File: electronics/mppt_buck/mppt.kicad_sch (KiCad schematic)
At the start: 50 parts, among them J1 I2C, J2 UART, J3 In, J4 In, J5 Out, J6 Out, Q1 IRLR2705TRPBF, Q2 IRLR2705TRPBF, SW1 SW_DIP_x01, U1 AD8211, U2 AD8211, U3 ATmega328P-A, U4 2EDN852x, U5 L78L15_SO8, Y1 16.00M-SMDHC49S

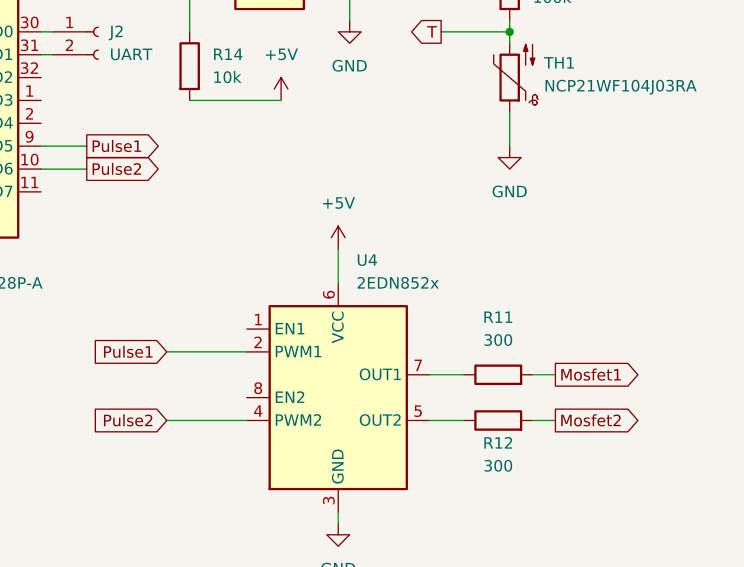
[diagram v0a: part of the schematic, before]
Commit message: links fixed
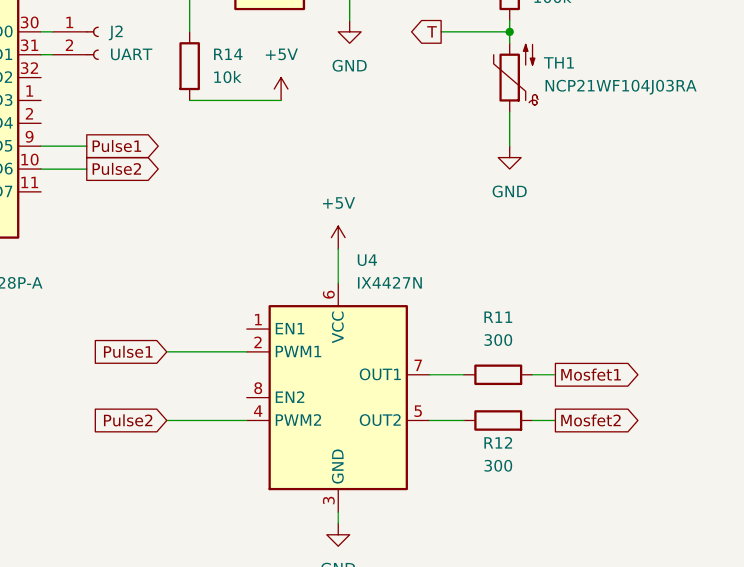
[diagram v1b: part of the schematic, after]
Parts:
- U4: value 2EDN852x -> IX4427N
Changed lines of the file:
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@@
       (effects (font (size 1.27 1.27)) hide)
     )
-    (property "Datasheet" "https://www.tme.eu/pl/details/t491d106k050at/kondensatory-tantalowe-smd/kemet/" (id 3) (at 33.02 137.16 0)
+    (property "Datasheet" "https://www.tme.eu/pl/details/vs1h100mc054000ce0/kondensatory-elektrolityczne-smd/changzhou-huawei-electronic/" (id 3) (at 33.02 137.16 0)
       (effects (font (size 1.27 1.27)) hide)
     )
@@
       (effects (font (size 1.27 1.27)) hide)
     )
-    (property "Datasheet" "https://www.tme.eu/pl/details/t491x226k050at/kondensatory-tantalowe-smd/kemet/" (id 3) (at 104.14 139.7 0)
+    (property "Datasheet" "https://www.tme.eu/pl/details/eee1ha220wp/kondensatory-elektrolityczne-smd/panasonic/" (id 3) (at 104.14 139.7 0)
       (effects (font (size 1.27 1.27)) hide)
     )
@@
       (effects (font (size 1.27 1.27)) hide)
     )
-    (property "Datasheet" "https://www.tme.eu/pl/details/t491d106k050at/kondensatory-tantalowe-smd/kemet/" (id 3) (at 31.75 66.04 0)
+    (property "Datasheet" "https://www.tme.eu/pl/details/vs1h100mc054000ce0/kondensatory-elektrolityczne-smd/changzhou-huawei-electronic/" (id 3) (at 31.75 66.04 0)
       (effects (font (size 1.27 1.27)) hide)
     )
@@
       (effects (font (size 1.27 1.27)) hide)
     )
-    (property "Datasheet" "https://www.tme.eu/pl/details/t491x226k050at/kondensatory-tantalowe-smd/kemet/" (id 3) (at 102.87 68.58 0)
+    (property "Datasheet" "https://www.tme.eu/pl/details/eee1ha220wp/kondensatory-elektrolityczne-smd/panasonic/" (id 3) (at 102.87 68.58 0)
       (effects (font (size 1.27 1.27)) hide)
     )
@@
       (effects (font (size 1.27 1.27) italic) hide)
     )
-    (property "Datasheet" "http://www.st.com/content/ccc/resource/technical/document/datasheet/15/55/e5/aa/23/5b/43/fd/CD00000446.pdf/files/CD00000446.pdf/jcr:content/translations/en.CD00000446.pdf" (id 3) (at 267.97 46.99 0)
+    (property "Datasheet" "https://www.tme.eu/pl/details/l78l15cd-tr/stabilizatory-napiecia-nieregulowane/stmicroelectronics/" (id 3) (at 267.97 46.99 0)
       (effects (font (size 1.27 1.27)) hide)
     )
@@
       (effects (font (size 1.27 1.27)) (justify left))
     )
-    (property "Value" "2EDN852x" (id 1) (at 247.1294 113.03 0)
+    (property "Value" "IX4427N" (id 1) (at 247.1294 113.03 0)
       (effects (font (size 1.27 1.27)) (justify left))
     )
@@
       (effects (font (size 1.27 1.27)) hide)
     )
-    (property "Datasheet" "http://www.st.com/resource/en/datasheet/pm8834.pdf" (id 3) (at 245.11 125.73 0)
+    (property "Datasheet" "https://www.tme.eu/pl/details/ix4427n/drivery-mosfet-igbt/ixys/" (id 3) (at 245.11 125.73 0)
       (effects (font (size 1.27 1.27)) hide)
     )
@@
     )
     (path "/f34564fb-d64a-449a-883e-a3d54ee9a0c7"
-      (reference "U4") (unit 1) (value "2EDN852x") (footprint "Package_SO:SOIC-8_3.9x4.9mm_P1.27mm")
+      (reference "U4") (unit 1) (value "IX4427N") (footprint "Package_SO:SOIC-8_3.9x4.9mm_P1.27mm")
     )
     (path "/e1c2f98d-65b5-4f1f-ae31-d3d1a6b636f5"

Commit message: links almost fixed finally
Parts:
- U1, U2: value AD8211 -> INA180A4IDBVT
- U5: value L78L15_SO8 -> DI78L05DAB
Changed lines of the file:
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@@
     (in_bom yes) (on_board yes) (fields_autoplaced)
     (property "Reference" "U2" (id 0) (at 105.41 98.3105 0))
-    (property "Value" "AD8211" (id 1) (at 105.41 100.8505 0))
+    (property "Value" "INA180A4IDBVT" (id 1) (at 105.41 100.8505 0))
     (property "Footprint" "Package_TO_SOT_SMD:SOT-23-5" (id 2) (at 118.11 109.22 0)
       (effects (font (size 1.27 1.27)) hide)
     )
-    (property "Datasheet" "https://www.tme.eu/pl/details/ad8211yrjz-r2/wzmacniacze-operacyjne-smd/analog-devices/" (id 3) (at 134.62 91.44 0)
+    (property "Datasheet" "https://www.tme.eu/pl/details/ina180a4idbvt/wzmacniacze-operacyjne-smd/texas-instruments/" (id 3) (at 134.62 91.44 0)
       (effects (font (size 1.27 1.27)) hide)
     )
@@
     (in_bom yes) (on_board yes) (fields_autoplaced)
     (property "Reference" "U1" (id 0) (at 104.14 27.1905 0))
-    (property "Value" "AD8211" (id 1) (at 104.14 29.7305 0))
+    (property "Value" "INA180A4IDBVT" (id 1) (at 104.14 29.7305 0))
     (property "Footprint" "Package_TO_SOT_SMD:SOT-23-5" (id 2) (at 116.84 38.1 0)
       (effects (font (size 1.27 1.27)) hide)
     )
-    (property "Datasheet" "https://www.tme.eu/pl/details/ad8211yrjz-r2/wzmacniacze-operacyjne-smd/analog-devices/" (id 3) (at 133.35 20.32 0)
+    (property "Datasheet" "https://www.tme.eu/pl/details/ina180a4idbvt/wzmacniacze-operacyjne-smd/texas-instruments/" (id 3) (at 133.35 20.32 0)
       (effects (font (size 1.27 1.27)) hide)
     )
@@
     (in_bom yes) (on_board yes) (fields_autoplaced)
     (property "Reference" "U5" (id 0) (at 262.89 39.37 0))
-    (property "Value" "L78L15_SO8" (id 1) (at 262.89 41.91 0))
+    (property "Value" "DI78L05DAB" (id 1) (at 262.89 41.91 0))
     (property "Footprint" "Package_SO:SOIC-8_3.9x4.9mm_P1.27mm" (id 2) (at 265.43 41.91 0)
       (effects (font (size 1.27 1.27) italic) hide)
     )
-    (property "Datasheet" "https://www.tme.eu/pl/details/l78l15cd-tr/stabilizatory-napiecia-nieregulowane/stmicroelectronics/" (id 3) (at 267.97 46.99 0)
+    (property "Datasheet" "https://www.tme.eu/pl/details/di78l05dab-dio/stabilizatory-napiecia-nieregulowane/diotec-semiconductor/di78l05dab/" (id 3) (at 267.97 46.99 0)
       (effects (font (size 1.27 1.27)) hide)
     )
@@
     )
     (path "/98f6b66c-5996-461c-b7fb-355b97b82833"
-      (reference "U1") (unit 1) (value "AD8211") (footprint "Package_TO_SOT_SMD:SOT-23-5")
+      (reference "U1") (unit 1) (value "INA180A4IDBVT") (footprint "Package_TO_SOT_SMD:SOT-23-5")
     )
     (path "/4613b16e-f85f-4ff8-be22-af836321faaf"
-      (reference "U2") (unit 1) (value "AD8211") (footprint "Package_TO_SOT_SMD:SOT-23-5")
+      (reference "U2") (unit 1) (value "INA180A4IDBVT") (footprint "Package_TO_SOT_SMD:SOT-23-5")
     )
     (path "/4efefe47-8389-4ee5-9e21-0623814e6216"
@@
     )
     (path "/e1c2f98d-65b5-4f1f-ae31-d3d1a6b636f5"
-      (reference "U5") (unit 1) (value "L78L15_SO8") (footprint "Package_SO:SOIC-8_3.9x4.9mm_P1.27mm")
+      (reference "U5") (unit 1) (value "DI78L05DAB") (footprint "Package_SO:SOIC-8_3.9x4.9mm_P1.27mm")
     )
     (path "/4fe02d41-b24c-4ab7-a3f5-8f451d9bcad9"

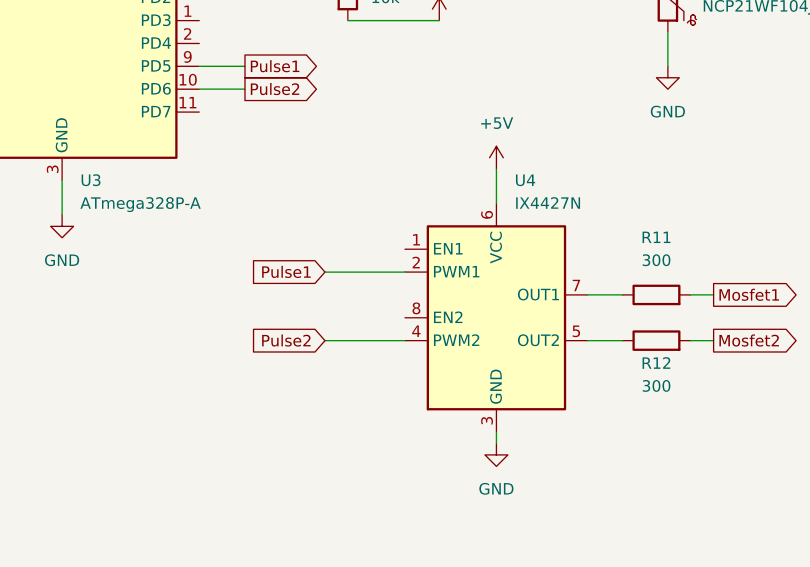
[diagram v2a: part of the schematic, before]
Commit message: mppt part list corrected
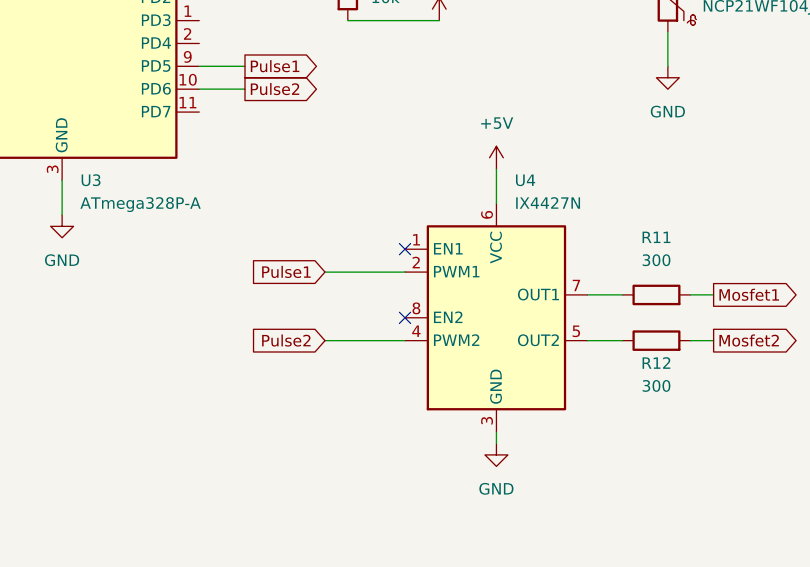
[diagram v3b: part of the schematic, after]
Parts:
- C1, C2: footprint Capacitor_Tantalum_SMD:CP_EIA-7343-15_Kemet-W_Pad2.25x2.55mm_HandSolder -> Capacitor_SMD:CP_Elec_5x5.4
- C3, C4: footprint Capacitor_Tantalum_SMD:CP_EIA-7343-15_Kemet-W_Pad2.25x2.55mm_HandSolder -> Capacitor_SMD:CP_Elec_6.3x5.4
- L1, L2: footprint Inductor_SMD:L_Bourns_SRR1208_12.7x12.7mm -> Inductor_SMD:L_10.4x10.4_H4.8
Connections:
- no-connect marks 0 -> 2
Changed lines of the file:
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@@
   (junction (at 82.55 67.31) (diameter 0) (color 0 0 0 0)
   )
+  (no_connect (at 234.95 118.11))
+  (no_connect (at 234.95 125.73))
   (wire (pts (xy 212.09 67.31) (xy 217.17 67.31))
     (stroke (width 0) (type default) (color 0 0 0 0))
@@
       (effects (font (size 1.27 1.27)) (justify left))
     )
-    (property "Footprint" "Capacitor_Tantalum_SMD:CP_EIA-7343-15_Kemet-W_Pad2.25x2.55mm_HandSolder" (id 2) (at 33.9852 140.97 0)
+    (property "Footprint" "Capacitor_SMD:CP_Elec_5x5.4" (id 2) (at 33.9852 140.97 0)
       (effects (font (size 1.27 1.27)) hide)
     )
@@
       (effects (font (size 1.27 1.27)) (justify left))
     )
-    (property "Footprint" "Capacitor_Tantalum_SMD:CP_EIA-7343-15_Kemet-W_Pad2.25x2.55mm_HandSolder" (id 2) (at 105.1052 143.51 0)
+    (property "Footprint" "Capacitor_SMD:CP_Elec_6.3x5.4" (id 2) (at 105.1052 143.51 0)
       (effects (font (size 1.27 1.27)) hide)
     )
@@
     (property "Reference" "L2" (id 0) (at 97.79 123.19 0))
     (property "Value" "100u" (id 1) (at 97.79 125.73 0))
-    (property "Footprint" "Inductor_SMD:L_Bourns_SRR1208_12.7x12.7mm" (id 2) (at 97.79 129.54 0)
-      (effects (font (size 1.27 1.27)) hide)
-    )
-    (property "Datasheet" "https://www.tme.eu/pl/details/de1205-100/dlawiki-smd-mocy/ferrocore/" (id 3) (at 97.79 129.54 0)
+    (property "Footprint" "Inductor_SMD:L_10.4x10.4_H4.8" (id 2) (at 97.79 129.54 0)
+      (effects (font (size 1.27 1.27)) hide)
+    )
+    (property "Datasheet" "https://www.tme.eu/pl/details/psdb1004nt101/dlawiki-smd-mocy/viking/" (id 3) (at 97.79 129.54 0)
       (effects (font (size 1.27 1.27)) hide)
     )
@@
       (effects (font (size 1.27 1.27)) (justify left))
     )
-    (property "Footprint" "Capacitor_Tantalum_SMD:CP_EIA-7343-15_Kemet-W_Pad2.25x2.55mm_HandSolder" (id 2) (at 32.7152 69.85 0)
+    (property "Footprint" "Capacitor_SMD:CP_Elec_5x5.4" (id 2) (at 32.7152 69.85 0)
       (effects (font (size 1.27 1.27)) hide)
     )
@@
       (effects (font (size 1.27 1.27)) (justify left))
     )
-    (property "Footprint" "Capacitor_Tantalum_SMD:CP_EIA-7343-15_Kemet-W_Pad2.25x2.55mm_HandSolder" (id 2) (at 103.8352 72.39 0)
+    (property "Footprint" "Capacitor_SMD:CP_Elec_6.3x5.4" (id 2) (at 103.8352 72.39 0)
       (effects (font (size 1.27 1.27)) hide)
     )
@@
     (property "Reference" "L1" (id 0) (at 91.44 52.07 0))
     (property "Value" "100u" (id 1) (at 91.44 54.61 0))
-    (property "Footprint" "Inductor_SMD:L_Bourns_SRR1208_12.7x12.7mm" (id 2) (at 91.44 58.42 0)
-      (effects (font (size 1.27 1.27)) hide)
-    )
-    (property "Datasheet" "https://www.tme.eu/pl/details/de1205-100/dlawiki-smd-mocy/ferrocore/" (id 3) (at 91.44 58.42 0)
+    (property "Footprint" "Inductor_SMD:L_10.4x10.4_H4.8" (id 2) (at 91.44 58.42 0)
+      (effects (font (size 1.27 1.27)) hide)
+    )
+    (property "Datasheet" "https://www.tme.eu/pl/details/psdb1004nt101/dlawiki-smd-mocy/viking/" (id 3) (at 91.44 58.42 0)
       (effects (font (size 1.27 1.27)) hide)
     )
@@
     )
     (path "/47ae361a-4310-4583-826d-5c506796dca5"
-      (reference "C1") (unit 1) (value "10u") (footprint "Capacitor_Tantalum_SMD:CP_EIA-7343-15_Kemet-W_Pad2.25x2.55mm_HandSolder")
+      (reference "C1") (unit 1) (value "10u") (footprint "Capacitor_SMD:CP_Elec_5x5.4")
     )
     (path "/00c033e4-0d1b-4741-a967-91ecefd9e56e"
-      (reference "C2") (unit 1) (value "10u") (footprint "Capacitor_Tantalum_SMD:CP_EIA-7343-15_Kemet-W_Pad2.25x2.55mm_HandSolder")
+      (reference "C2") (unit 1) (value "10u") (footprint "Capacitor_SMD:CP_Elec_5x5.4")
     )
     (path "/ccff23da-53f9-49bf-b916-584eea475766"
-      (reference "C3") (unit 1) (value "22u") (footprint "Capacitor_Tantalum_SMD:CP_EIA-7343-15_Kemet-W_Pad2.25x2.55mm_HandSolder")
+      (reference "C3") (unit 1) (value "22u") (footprint "Capacitor_SMD:CP_Elec_6.3x5.4")
     )
     (path "/017c4ae8-dd6c-4ee2-b898-cf2df1f93d8c"
-      (reference "C4") (unit 1) (value "22u") (footprint "Capacitor_Tantalum_SMD:CP_EIA-7343-15_Kemet-W_Pad2.25x2.55mm_HandSolder")
+      (reference "C4") (unit 1) (value "22u") (footprint "Capacitor_SMD:CP_Elec_6.3x5.4")
     )
     (path "/c21981ba-d479-4332-a264-478bfdfd7198"
@@
     )
     (path "/ecfb3e89-3197-4516-87f6-ebd0029fde13"
-      (reference "L1") (unit 1) (value "100u") (footprint "Inductor_SMD:L_Bourns_SRR1208_12.7x12.7mm")
+      (reference "L1") (unit 1) (value "100u") (footprint "Inductor_SMD:L_10.4x10.4_H4.8")
     )
     (path "/25d0d534-6408-4778-8ce4-918863d27fa7"
-      (reference "L2") (unit 1) (value "100u") (footprint "Inductor_SMD:L_Bourns_SRR1208_12.7x12.7mm")
+      (reference "L2") (unit 1) (value "100u") (footprint "Inductor_SMD:L_10.4x10.4_H4.8")
     )
     (path "/bcb85753-aaa1-4007-936a-fba0292daa8e"
